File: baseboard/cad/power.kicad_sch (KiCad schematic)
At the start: 33 parts, among them U7 TLV767, U8 LT3463, U9 LT3032

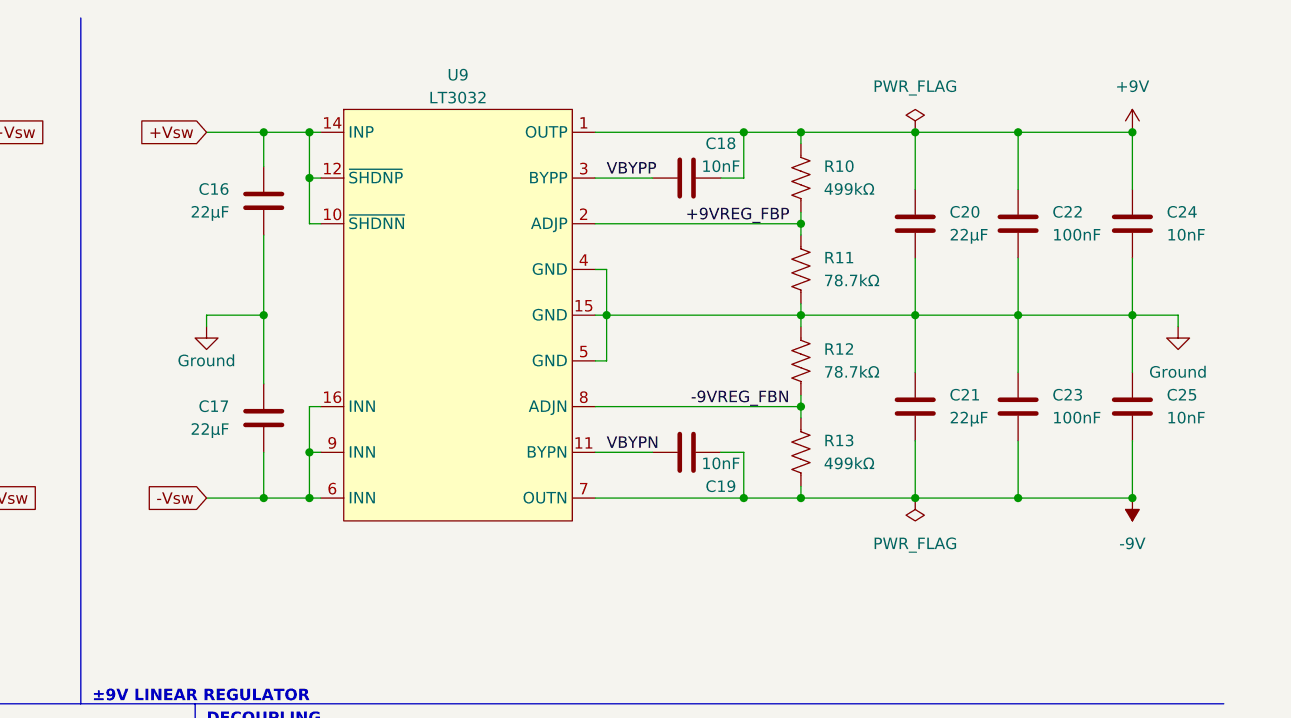
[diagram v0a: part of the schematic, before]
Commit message: added microcontroller enable to analog power rails
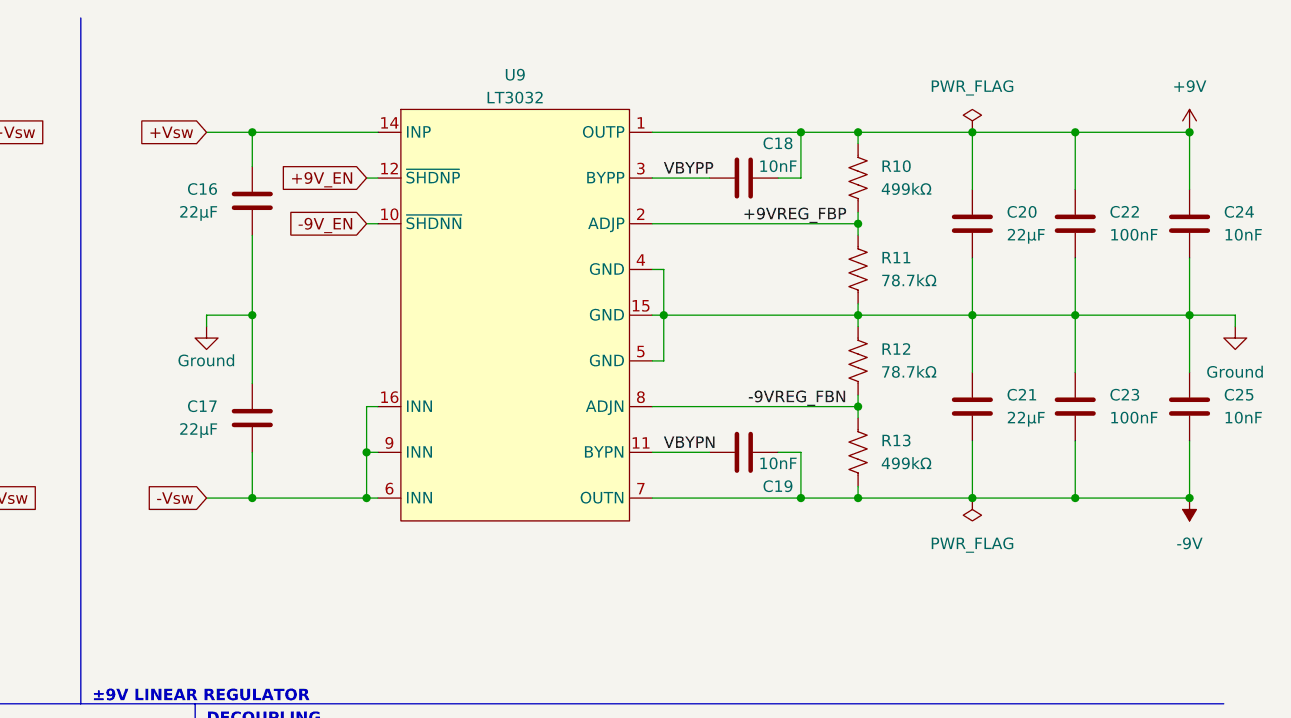
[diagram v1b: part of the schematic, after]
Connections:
- net +Vsw: no longer U9.10 (~{SHDNN}), U9.12 (~{SHDNP})
- new net +9V_EN: U9.12 (~{SHDNP})
- new net -9V_EN: U9.10 (~{SHDNN})
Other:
- moved on the sheet: C16, C17, C18, C19, C20, C21, C22, C23, C24, C25, R10, R11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

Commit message: added reset button to microcontroller
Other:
- note removed: "DECOUPLING"
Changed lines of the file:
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@@
-    (stroke (width 0) (type default))
-  )
-  (polyline (pts (xy 139.7 101.6) (xy 139.7 177.8))
     (stroke (width 0) (type default))
   )
@@
     (effects (font (size 1.27 1.27) bold) (justify left bottom))
   )
-  (text "DECOUPLING" (at 140.97 104.14 0)
-    (effects (font (size 1.27 1.27) (thickness 0.254) bold) (justify left bottom))
-  )
   (text "+3.3V LINEAR REGULATOR" (at 26.67 104.14 0)

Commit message: swapped micro and started layout
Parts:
- U8: footprint Package_DFN_QFN:DFN-10-1EP_3x3mm_P0.5mm_EP1.65x2.38mm -> Package_DFN_QFN:DFN-10-1EP_3x3mm_P0.5mm_EP1.65x2.38mm_ThermalVias
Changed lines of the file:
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@@
       (effects (font (size 1.27 1.27)))
     )
-    (property "Footprint" "Package_DFN_QFN:DFN-10-1EP_3x3mm_P0.5mm_EP1.65x2.38mm" (at 67.818 50.292 0)
+    (property "Footprint" "Package_DFN_QFN:DFN-10-1EP_3x3mm_P0.5mm_EP1.65x2.38mm_ThermalVias" (at 67.818 50.292 0)
       (effects (font (size 1.27 1.27)) hide)
     )

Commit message: placed components and finished new micro hw
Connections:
- net +Vsw: no longer C12.2, U7.4 (EN), U7.6 (IN)
- net DC_IN: now also C12.2, U7.4 (EN), U7.6 (IN); no longer U8.8 (~{SHDN2}), U8.9 (~{SHDN1})
- new net +12V_EN: U8.9 (~{SHDN1})
- new net -12V_EN: U8.8 (~{SHDN2})
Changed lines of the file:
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@@
   (junction (at 107.95 78.74) (diameter 0) (color 0 0 0 0)
   )
-  (junction (at 53.34 38.1) (diameter 0) (color 0 0 0 0)
-  )
   (junction (at 91.44 78.74) (diameter 0) (color 0 0 0 0)
   )
@@
   (junction (at 78.74 137.16) (diameter 0) (color 0 0 0 0)
   )
-  (junction (at 53.34 43.18) (diameter 0) (color 0 0 0 0)
-  )
   (junction (at 213.36 38.1) (diameter 0) (color 0 0 0 0)
   )
@@
     (stroke (width 0) (type default))
   )
-  (wire (pts (xy 39.37 38.1) (xy 53.34 38.1))
+  (wire (pts (xy 39.37 38.1) (xy 54.61 38.1))
     (stroke (width 0) (type default))
   )
@@
     (stroke (width 0) (type default))
   )
-  (wire (pts (xy 53.34 38.1) (xy 54.61 38.1))
-    (stroke (width 0) (type default))
-  )
   (wire (pts (xy 95.25 78.74) (xy 107.95 78.74))
     (stroke (width 0) (type default))
@@
     (stroke (width 0) (type default))
   )
-  (wire (pts (xy 53.34 48.26) (xy 53.34 43.18))
-    (stroke (width 0) (type default))
-  )
   (wire (pts (xy 29.21 38.1) (xy 29.21 40.64))
     (stroke (width 0) (type default))
@@
   )
   (wire (pts (xy 226.06 44.45) (xy 226.06 38.1))
-    (stroke (width 0) (type default))
-  )
-  (wire (pts (xy 53.34 43.18) (xy 53.34 38.1))
     (stroke (width 0) (type default))
   )
@@
     (effects (font (size 1.27 1.27)) (justify left bottom))
   )
-  (global_label "+Vsw" (shape input) (at 36.83 124.46 180) (fields_autoplaced)
+  (global_label "DC_IN" (shape input) (at 36.83 124.46 180) (fields_autoplaced)
     (effects (font (size 1.27 1.27)) (justify right))
-    (property "Intersheetrefs" "${INTERSHEET_REFS}" (at 29.3974 124.5394 0)
+    (property "Intersheetrefs" "${INTERSHEET_REFS}" (at 28.7382 124.46 0)
       (effects (font (size 1.27 1.27)) (justify right) hide)
     )
@@
     )
   )
+  (global_label "+12V_EN" (shape input) (at 53.34 43.18 180) (fields_autoplaced)
+    (effects (font (size 1.27 1.27)) (justify right))
+    (property "Intersheetrefs" "${INTERSHEET_REFS}" (at 43.1166 43.18 0)
+      (effects (font (size 1.27 1.27)) (justify right) hide)
+    )
+  )
   (global_label "+Vsw" (shape input) (at 115.57 38.1 0) (fields_autoplaced)
     (effects (font (size 1.27 1.27)) (justify left))
@@
     (effects (font (size 1.27 1.27)) (justify right))
     (property "Intersheetrefs" "${INTERSHEET_REFS}" (at 133.5374 38.0206 0)
+      (effects (font (size 1.27 1.27)) (justify right) hide)
+    )
+  )
+  (global_label "-12V_EN" (shape input) (at 53.34 48.26 180) (fields_autoplaced)
+    (effects (font (size 1.27 1.27)) (justify right))
+    (property "Intersheetrefs" "${INTERSHEET_REFS}" (at 43.1166 48.26 0)
       (effects (font (size 1.27 1.27)) (justify right) hide)
     )
@@
   (symbol (lib_id "Device:L") (at 44.45 58.42 90) (unit 1)
     (in_bom yes) (on_board yes) (dnp no)
-    (property "Reference" "L2" (at 44.45 60.96 90)
-      (effects (font (size 1.27 1.27)))
-    )
-    (property "Value" "15μH" (at 44.45 63.5 90)
+    (property "Reference" "L2" (at 44.45 59.69 90)
+      (effects (font (size 1.27 1.27)))
+    )
+    (property "Value" "15μH" (at 44.45 60.96 90)
       (effects (font (size 1.27 1.27)))
     )
@@
   )
   (symbol (lib_id "Device:L") (at 44.45 53.34 270) (mirror x) (unit 1)
-    (in_bom yes) (on_board yes) (dnp no) (fields_autoplaced)
-    (property "Reference" "L1" (at 44.45 46.99 90)
-      (effects (font (size 1.27 1.27)))
-    )
-    (property "Value" "15μH" (at 44.45 49.53 90)
-      (effects (font (size 1.27 1.27)))
-    )
+    (in_bom yes) (on_board yes) (dnp no)
+    (property "Reference" "L1" (at 44.45 54.61 90)
+      (effects (font (size 1.27 1.27)))
+    )
+    (property "Value" "15μH" (at 44.45 55.88 90)
+      (effects (font (size 1.27 1.27)))
+    )

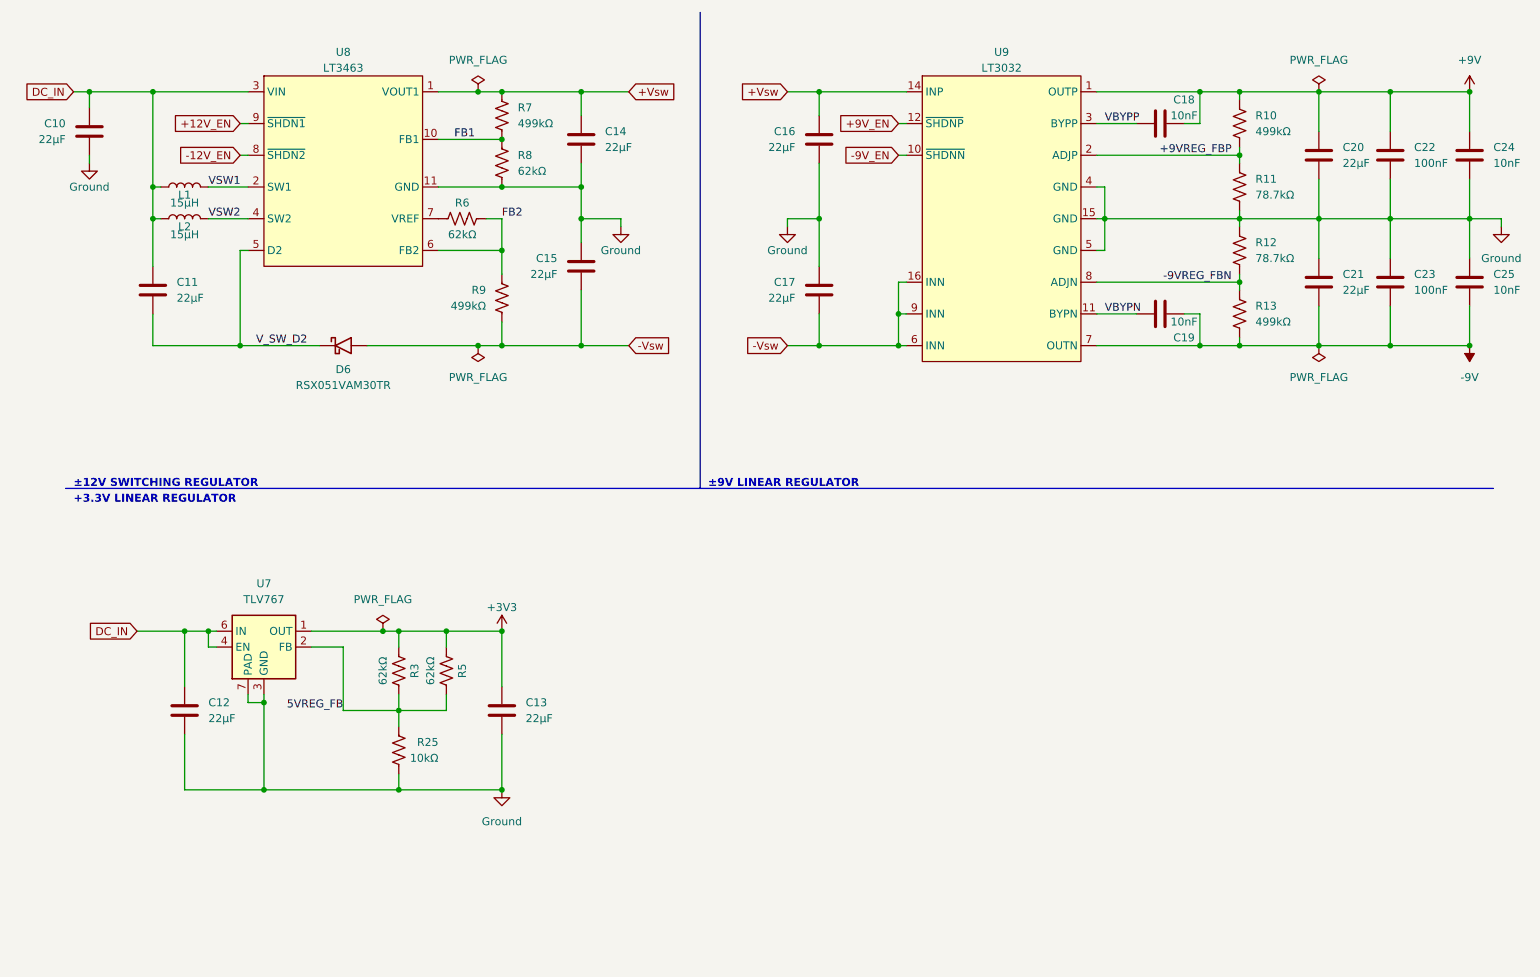
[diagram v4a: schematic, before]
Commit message: swapped relays for nice analog switch, saved $4
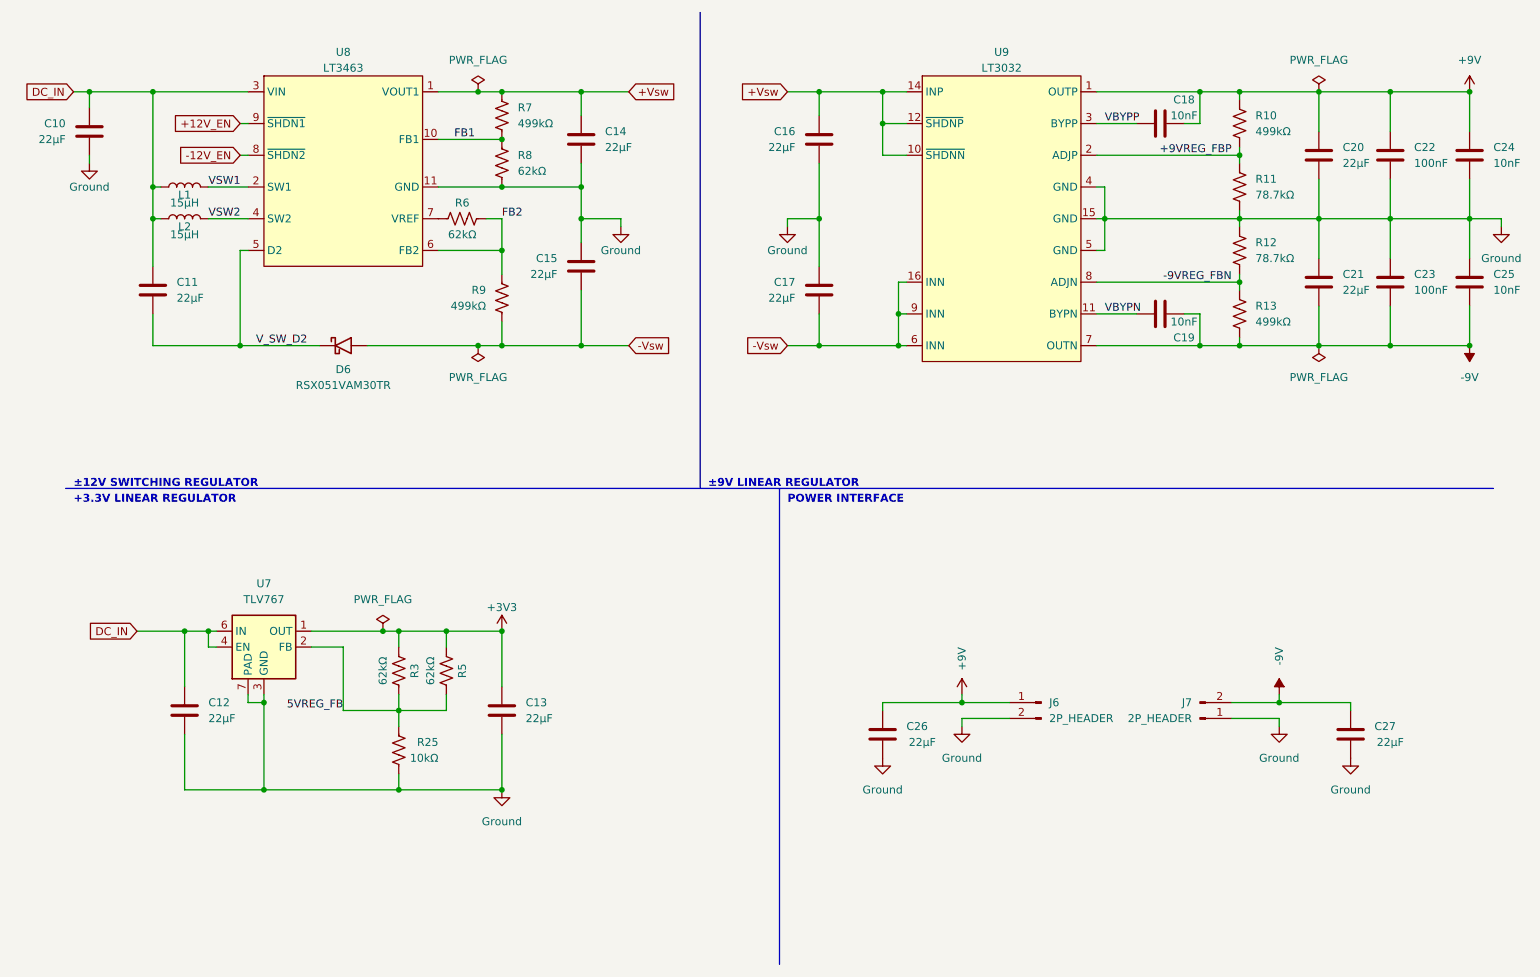
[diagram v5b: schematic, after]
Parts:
- added C26, C27: 22μF, Capacitor_SMD:C_0805_2012Metric, symbol Device:C
- added J6, J7: 2P_HEADER, Connector_PinSocket_2.54mm:PinSocket_1x02_P2.54mm_Vertical, symbol Connector:Conn_01x02_Male
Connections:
- net +9V_EN is gone; now on net +Vsw: U9.12 (~{SHDNP})
- net -9V_EN is gone; now on net +Vsw: U9.10 (~{SHDNN})
- net +9V: now also C26.2, J6.1 (Pin_1)
- net -9V: now also C27.2, J7.2 (Pin_2)
- net GND: now also C26.1, C27.1, J6.2 (Pin_2), J7.1 (Pin_1)
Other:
- note added: "POWER INTERFACE"
